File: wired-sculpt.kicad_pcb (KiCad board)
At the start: 2 copper layers, 40 x 54 mm, 40 parts, among them J1 USB_C_Receptacle, J2 FFC3B07-30-T, J3 AVR-ISP-6 - NOT FITTED, Q1 BSS84AK,215, Q2 2N7002BK,215, SW1 EVQ-P7A01P, U1 USBLC6-2SC6, U2 LM2776DBVT, U3 AT90USB1286-AUR, Y1 TSX-3225 16.0000MF18X-AC0

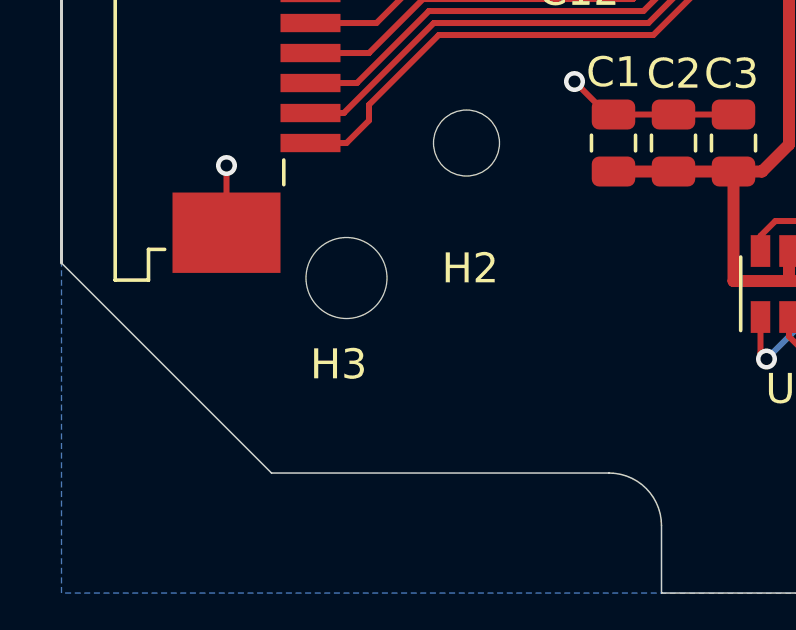
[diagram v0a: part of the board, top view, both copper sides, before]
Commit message: Increase H3 to 3mm
Slightly more tolerance is needed. Board fit in one of my keyboards, but
not the other
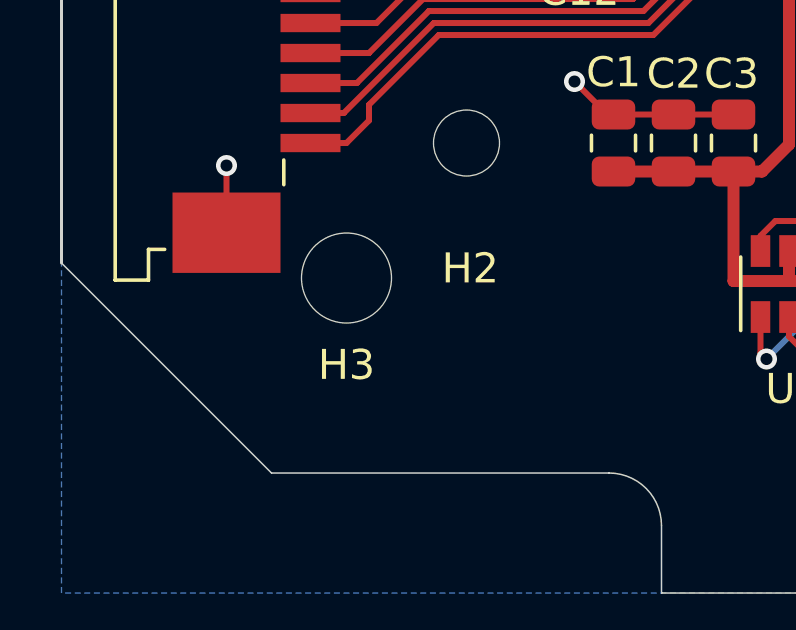
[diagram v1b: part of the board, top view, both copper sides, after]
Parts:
- H3: footprint MountingHole:MountingHole_2.7mm -> MountingHole:MountingHole_3mm
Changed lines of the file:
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@@
     )
   )
-  (footprint "MountingHole:MountingHole_2.7mm" (layer "F.Cu")
+  (footprint "MountingHole:MountingHole_3mm" (layer "F.Cu")
     (at 129.5 73.5)
-    (descr "Mounting Hole 2.7mm, no annular")
-    (tags "mounting hole 2.7mm no annular")
+    (descr "Mounting Hole 3mm, no annular")
+    (tags "mounting hole 3mm no annular")
     (property "Sheetfile" "wired-sculpt.kicad_sch")
     (property "Sheetname" "")
     (property "exclude_from_bom" "")
     (attr exclude_from_pos_files exclude_from_bom)
-    (fp_text reference "H3" (at -0.26 2.88) (layer "F.SilkS")
+    (fp_text reference "H3" (at 0 2.9) (layer "F.SilkS")
       (effects (font (size 1 1) (thickness 0.15)))
     )
-    (fp_text value "AlignmentHole" (at 0 3.7) (layer "F.Fab")
+    (fp_text value "AlignmentHole" (at 0 4) (layer "F.Fab")
       (effects (font (size 1 1) (thickness 0.15)))
     )
-    (fp_text user "${REFERENCE}" (at 0.3 0) (layer "F.Fab")
+    (fp_text user "${REFERENCE}" (at 0 0) (layer "F.Fab")
       (effects (font (size 1 1) (thickness 0.15)))
     )
-    (fp_circle (center 0 0) (end 1.589547 0.091544) (layer "Cmts.User") (width 0.15) (fill none))
-    (fp_circle (center 0 0) (end 1.822569 0.099866) (layer "F.CrtYd") (width 0.05) (fill none))
-    (pad "" np_thru_hole circle (at 0 0) (size 2.7 2.7) (drill 2.7) (layers *.Cu *.Mask))
+    (fp_circle (center 0 0) (end 1.7 0) (layer "Cmts.User") (width 0.15) (fill none))
+    (fp_circle (center 0 0) (end 1.8 0) (layer "F.CrtYd") (width 0.05) (fill none))
+    (pad "" np_thru_hole circle (at 0 0) (size 3 3) (drill 3) (layers *.Cu *.Mask))
   )
   (footprint "Resistor_SMD:R_0603_1608Metric" (layer "F.Cu")

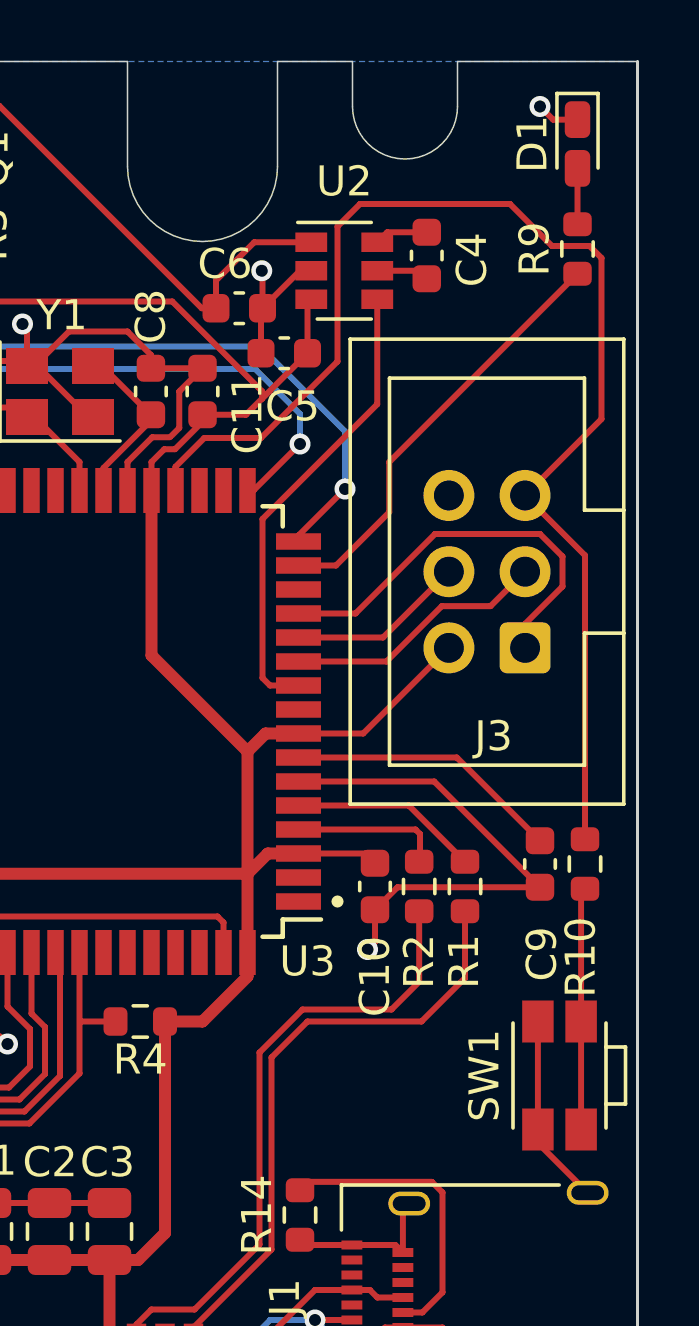
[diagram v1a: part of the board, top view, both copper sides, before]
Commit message: Remove on-board status LED
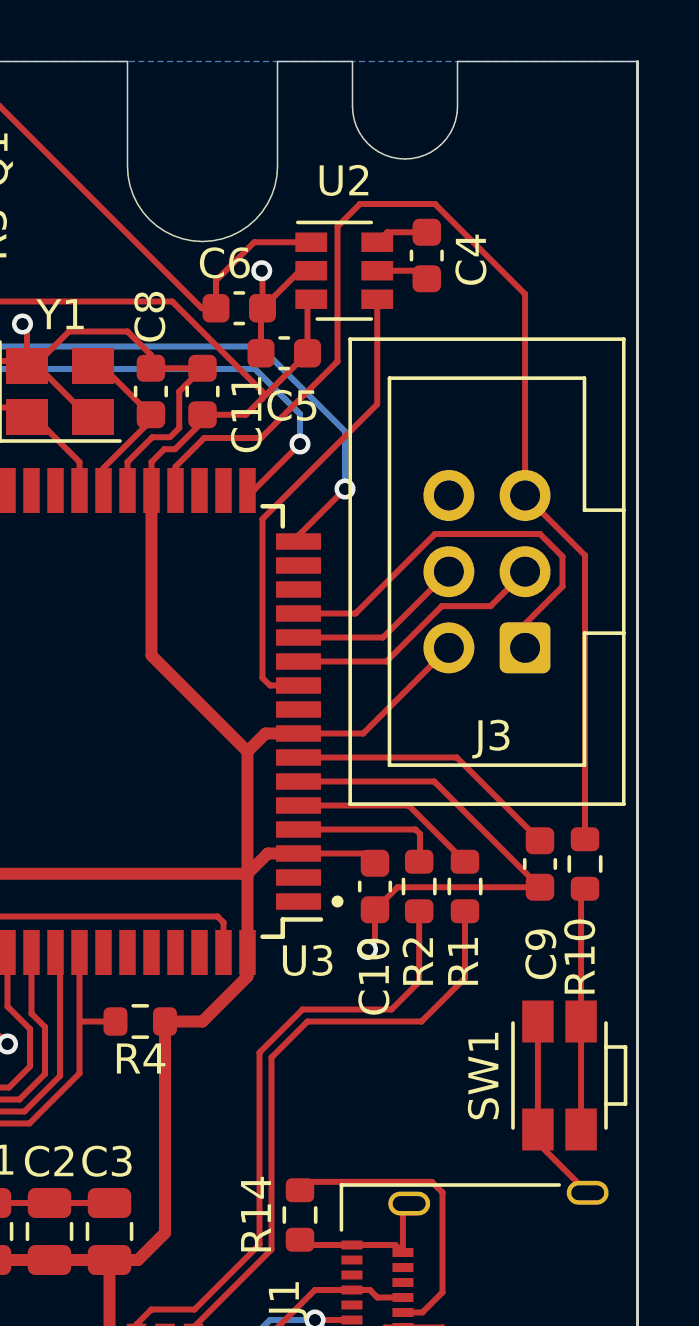
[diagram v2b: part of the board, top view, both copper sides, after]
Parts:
- removed D1: 150080GS75000, LED_SMD:LED_0603_1608Metric_Castellated
- removed R9: ERJ-3GEYJ331V, Resistor_SMD:R_0603_1608Metric
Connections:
- U3 pad 15: LED -> unconnected-(U3-Pad15)
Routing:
- net LED: track 14.3 -> 0.00 mm
- net RST: track 43.3 -> 39.0 mm
- net GND: track 85.7 -> 83.9 mm, vias 11 -> 10
- net Net-(D1-Pad2): track 1.86 -> 0.00 mm

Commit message: Bump on-board version number
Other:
- board text added: "Wired Sculpt 0.7"
- board text removed: "Wired Sculpt 0.6"
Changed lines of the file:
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@@
   (gr_line (start 140 84) (end 140 81.75) (layer "Edge.Cuts") (width 0.05))
   (gr_line (start 148 30) (end 148 33.5) (layer "Edge.Cuts") (width 0.05))
-  (gr_text "Wired Sculpt 0.6" (at 151.75 82.25) (layer "F.SilkS")
+  (gr_text "Wired Sculpt 0.7" (at 151.75 82.25) (layer "F.SilkS")
     (effects (font (size 0.7 0.7) (thickness 0.1)))
   )
